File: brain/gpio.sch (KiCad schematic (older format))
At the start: 46 parts

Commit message: footprint assignation
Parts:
- ANA0, ANA1, ANA2, ANA3, ANA4, GPIO0, GPIO1, GPIO10, GPIO11, GPIO2, GPIO3, GPIO4, GPIO5, GPIO6, GPIO7, GPIO8, GPIO9: footprint (none) -> Sockets_MOLEX_KK-System:Socket_MOLEX-KK-RM2-54mm_Lock_3pin_straight
- C57, C58, C59, C60, C61, C62, C63, C64, C65, C66, C67, C68, C69: renamed from C?; footprint (none) -> Capacitors_SMD:C_0603
- COLOR1: renamed from COLOR; footprint (none) -> Sockets_MOLEX_KK-System:Socket_MOLEX-KK-RM2-54mm_Lock_3pin_straight
- R17, R18, R19, R20, R21, R22, R23, R24, R25, R26, R27, R28: renamed from R?; footprint (none) -> Resistors_SMD:R_0603
- SHIFTREG1: renamed from SHIFTREG; footprint (none) -> Sockets_MOLEX_KK-System:Socket_MOLEX-KK-RM2-54mm_Lock_6pin_straight
- STARTER1: renamed from STARTER; footprint (none) -> Sockets_MOLEX_KK-System:Socket_MOLEX-KK-RM2-54mm_Lock_3pin_straight
- U7: renamed from U?; footprint (none) -> Housings_SSOP:TSSOP-20_4.4x6.5mm_Pitch0.65mm
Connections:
- wire segments 169 -> 172

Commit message: Brain 2018 layout
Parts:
- C57, C58, C59, C60, C61, C62, C63, C64, C65, C66, C67, C68, C69: symbol C -> C-RESCUE-brain
- R17, R18, R19, R20, R21, R22, R23, R24, R25, R26, R27, R28: symbol R -> R-RESCUE-brain

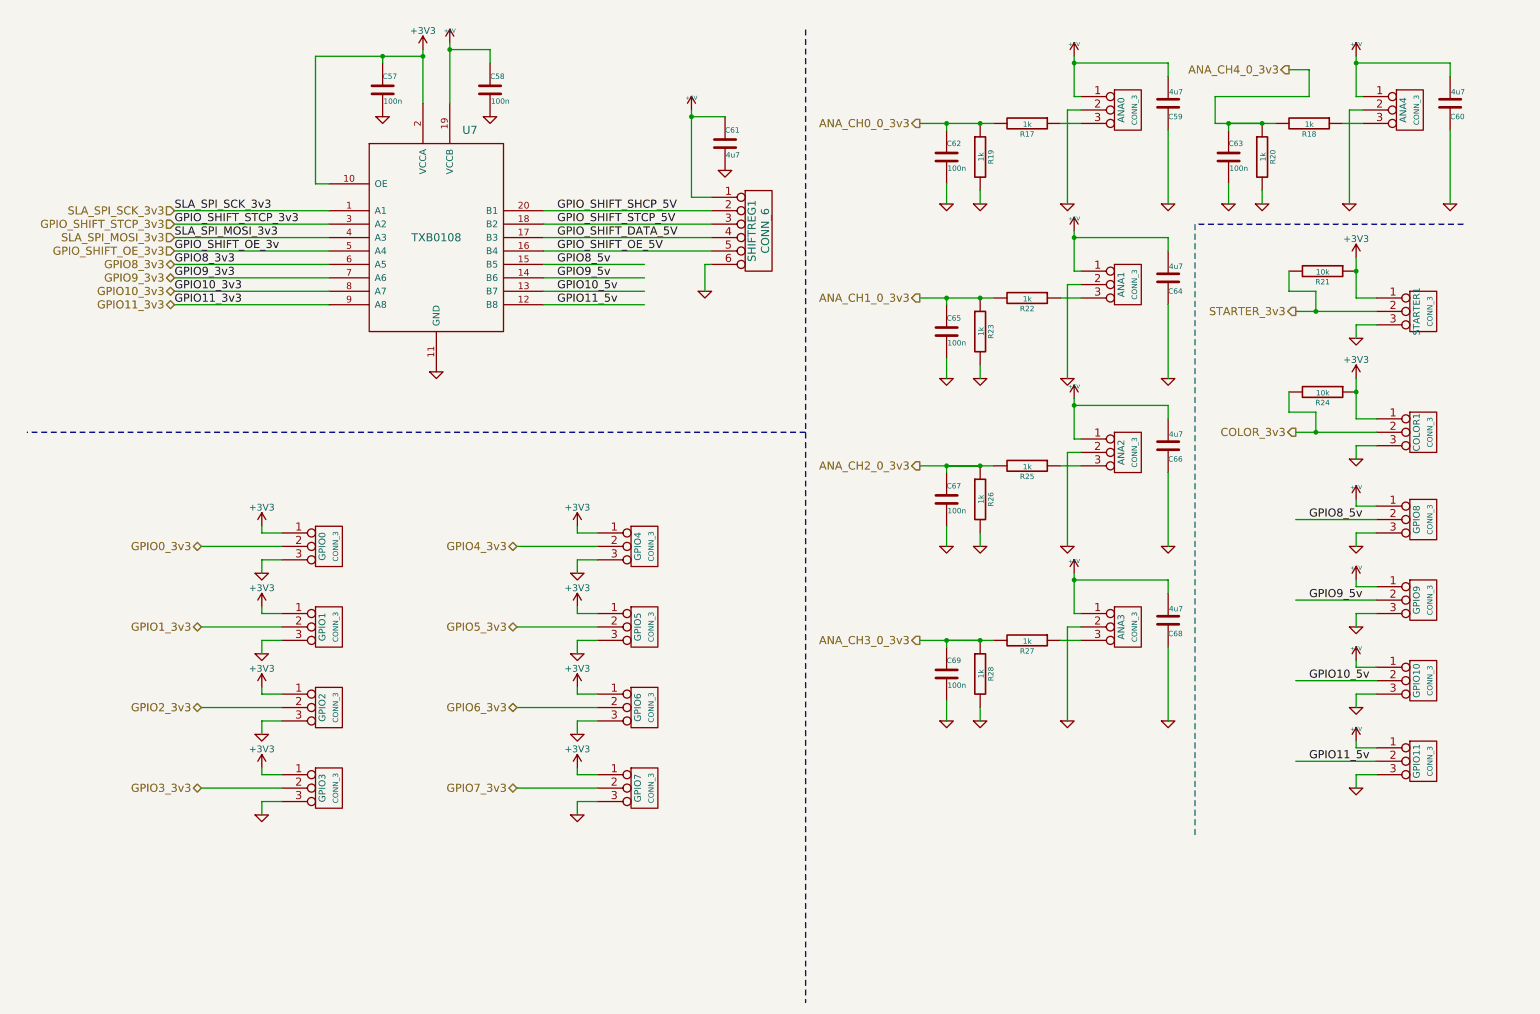
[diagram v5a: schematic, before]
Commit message: change shift register connector to match Cocoout and Cocoin
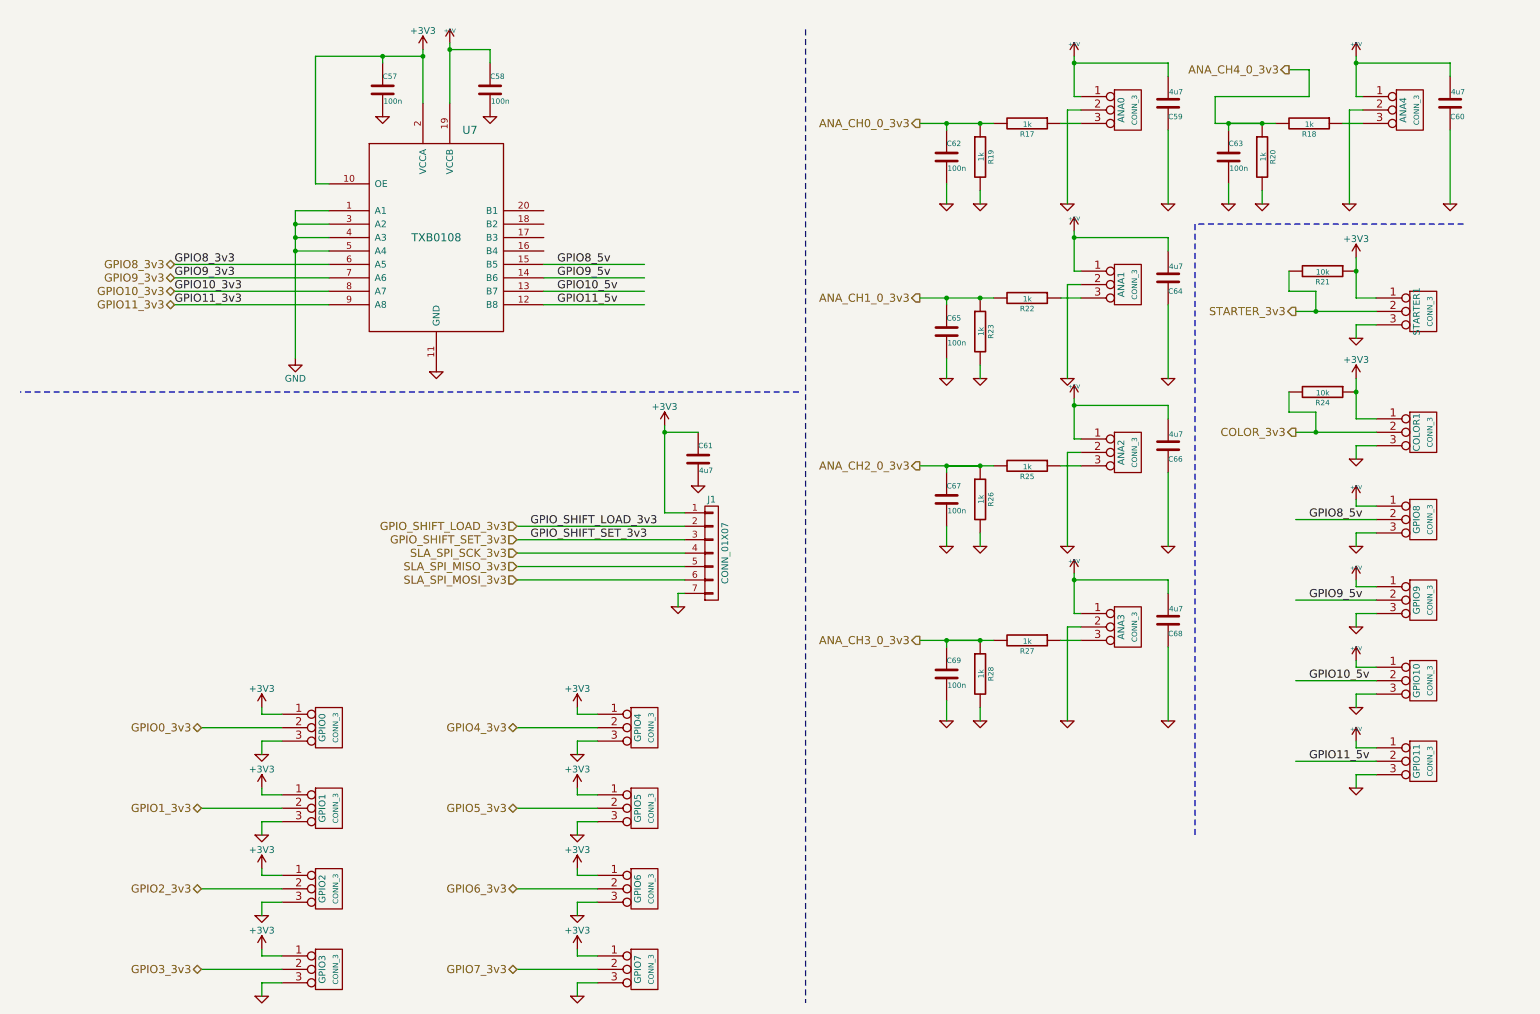
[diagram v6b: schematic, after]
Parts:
- removed SHIFTREG1: CONN_6, Sockets_MOLEX_KK-System:Socket_MOLEX-KK-RM2-54mm_Lock_6pin_straight, symbol CONN_6
- added J1: CONN_01X07, espitall:Socket_MOLEX-KK-RM2-54mm_Lock_7pin_straight, symbol CONN_01X07
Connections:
- net labels added: GPIO_SHIFT_LOAD_3v3, GPIO_SHIFT_SET_3v3, SLA_SPI_MISO_3v3
- net labels removed: GPIO_SHIFT_DATA_5V, GPIO_SHIFT_OE_3v, GPIO_SHIFT_OE_3v3, GPIO_SHIFT_OE_5V, GPIO_SHIFT_SHCP_5V, GPIO_SHIFT_STCP_3v3, GPIO_SHIFT_STCP_5V
- wire segments 172 -> 174
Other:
- moved on the sheet: C61, GPIO0, GPIO1, GPIO2, GPIO3, GPIO4, GPIO5, GPIO6, GPIO7

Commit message: add 3d step files to brain
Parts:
- ANA0, ANA1, ANA2, ANA3, ANA4, COLOR1, GPIO0, GPIO1, GPIO10, GPIO11, GPIO2, GPIO3, GPIO4, GPIO5, GPIO6, GPIO7, GPIO8, GPIO9, STARTER1: footprint Sockets_MOLEX_KK-System:Socket_MOLEX-KK-RM2-54mm_Lock_3pin_straight -> espitall:Socket_MOLEX-KK-RM2-54mm_Lock_3pin_straight
- C57, C58, C59, C60, C61, C62, C63, C64, C65, C66, C67, C68, C69: footprint Capacitors_SMD:C_0603 -> espitall:C_0603
- R17, R18, R19, R20, R21, R22, R23, R24, R25, R26, R27, R28: footprint Resistors_SMD:R_0603 -> espitall:R_0603
- U7: footprint Housings_SSOP:TSSOP-20_4.4x6.5mm_Pitch0.65mm -> espitall:TSSOP-20_4.4x6.5mm_Pitch0.65mm

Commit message: add module add footprint SPSGRF-868 for future com board
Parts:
- ANA0, ANA1, ANA2, ANA3, ANA4, COLOR1, GPIO0, GPIO1, GPIO10, GPIO11, GPIO2, GPIO3, GPIO4, GPIO5, GPIO6, GPIO7, GPIO8, GPIO9, STARTER1: symbol CONN_3 -> brain-rescue:CONN_3-RESCUE-brain
- C57, C58, C59, C60, C61, C62, C63, C64, C65, C66, C67, C68, C69: symbol C-RESCUE-brain -> brain-rescue:C-RESCUE-brain
- J1: symbol CONN_01X07 -> brain-rescue:CONN_01X07-RESCUE-brain
- R17, R18, R19, R20, R21, R22, R23, R24, R25, R26, R27, R28: symbol R-RESCUE-brain -> brain-rescue:R-RESCUE-brain
- U7: symbol TXB0108 -> espitall:TXB0108
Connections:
- wire segments 174 -> 197
